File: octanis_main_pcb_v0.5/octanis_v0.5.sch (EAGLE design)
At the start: 80 parts, among them IC1 BME280, IC2 BNO055A, Q1 32.768kHz, Q2 32.768kHz, U1 MSP432, U2 TPS61232, U3 DRV8836DSSR, U4 DRV8836DSSR, U5 DRV8836DSSR, U6 DRV8836DSSR, U7 SST25VF064C

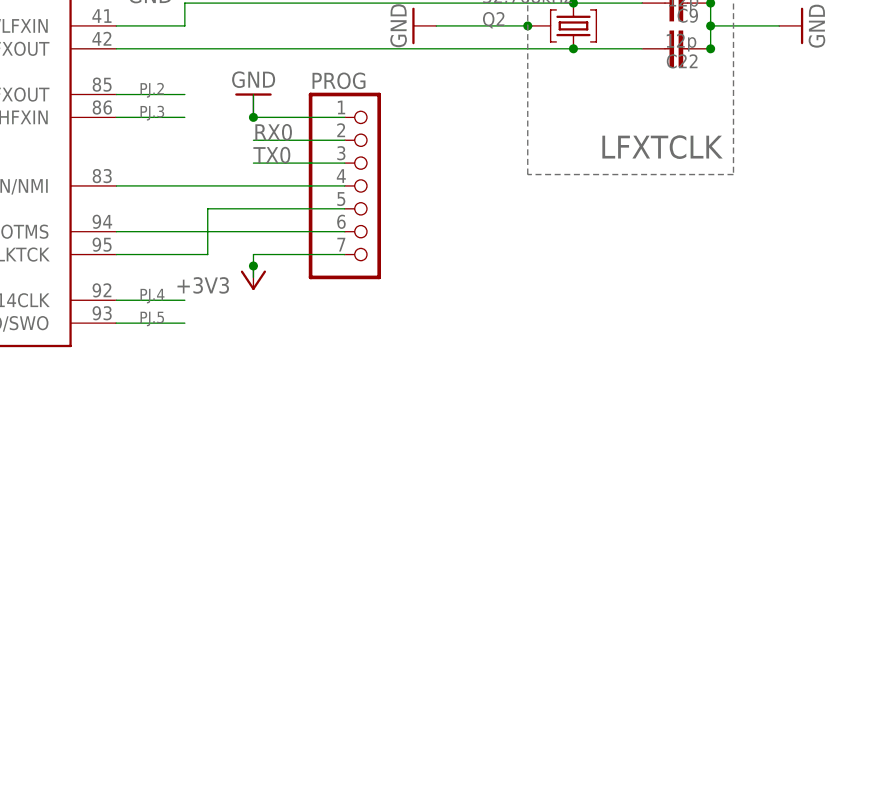
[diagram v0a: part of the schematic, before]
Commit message: added RST pull-up
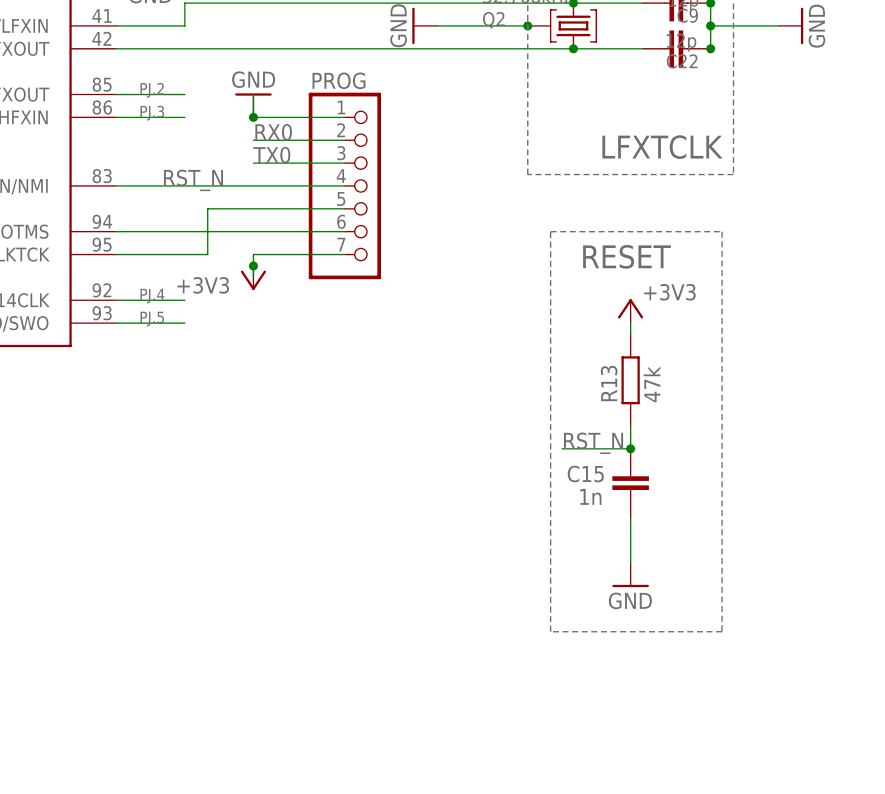
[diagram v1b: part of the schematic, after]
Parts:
- added C15: 1n, rcl:C-EUCM0402
- added R13: 47k, rcl:R-EU_RM0402
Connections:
- removed net N$75: PROG.4, U1.RSTN/NMI
- new net RST_N: C15.1, PROG.4, R13.1, U1.RSTN/NMI
- net +3V3: now also R13.2
- net GND: now also C15.2
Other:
- note added: "RESET"
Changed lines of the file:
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@@
 <part name="GND33" library="supply1" deviceset="GND" device=""/>
 <part name="GND34" library="supply1" deviceset="GND" device=""/>
+<part name="C15" library="rcl" deviceset="C-EU" device="CM0402" value="1n"/>
+<part name="GND40" library="supply1" deviceset="GND" device=""/>
+<part name="+3V25" library="supply1" deviceset="+3V3" device=""/>
+<part name="R13" library="rcl" deviceset="R-EU_" device="RM0402" value="47k"/>
 </parts>
 <sheets>
@@
 </text>
 <text x="228.6" y="228.6" size="1.27" layer="97">VeREF- (recommended to connect to GND)</text>
+<text x="424.942" y="188.976" size="2.54" layer="95">RESET</text>
+<wire x1="421.64" y1="148.59" x2="421.64" y2="193.04" width="0.1524" layer="95" style="shortdash"/>
+<wire x1="421.64" y1="193.04" x2="440.69" y2="193.04" width="0.1524" layer="95" style="shortdash"/>
+<wire x1="440.69" y1="193.04" x2="440.69" y2="148.59" width="0.1524" layer="95" style="shortdash"/>
+<wire x1="440.69" y1="148.59" x2="421.64" y2="148.59" width="0.1524" layer="95" style="shortdash"/>
 </plain>
 <instances>
@@
 <instance part="GND33" gate="1" x="205.74" y="215.9" rot="R90"/>
 <instance part="GND34" gate="1" x="266.7" y="228.6" rot="R270"/>
+<instance part="C15" gate="G$1" x="430.53" y="166.37" smashed="yes">
+<attribute name="NAME" x="423.418" y="165.227" size="1.778" layer="95"/>
+<attribute name="VALUE" x="424.688" y="162.687" size="1.778" layer="96"/>
+</instance>
+<instance part="GND40" gate="1" x="430.53" y="153.67"/>
+<instance part="+3V25" gate="G$1" x="430.53" y="185.42" smashed="yes">
+<attribute name="VALUE" x="431.8" y="185.42" size="1.778" layer="96"/>
+</instance>
+<instance part="R13" gate="G$1" x="430.53" y="176.53" smashed="yes" rot="R90">
+<attribute name="NAME" x="429.0314" y="173.99" size="1.778" layer="95" rot="R90"/>
+<attribute name="VALUE" x="433.832" y="173.99" size="1.778" layer="96" rot="R90"/>
+</instance>
 </instances>
 <busses>
@@
 <pinref part="GND8" gate="1" pin="GND"/>
 <wire x1="401.32" y1="299.72" x2="411.48" y2="299.72" width="0.1524" layer="91"/>
+</segment>
+<segment>
+<pinref part="GND40" gate="1" pin="GND"/>
+<pinref part="C15" gate="G$1" pin="2"/>
+<wire x1="430.53" y1="156.21" x2="430.53" y2="158.75" width="0.1524" layer="91"/>
+<wire x1="430.53" y1="158.75" x2="430.53" y2="161.29" width="0.1524" layer="91"/>
 </segment>
 </net>
@@
 <wire x1="398.78" y1="297.18" x2="411.48" y2="297.18" width="0.1524" layer="91"/>
 </segment>
+<segment>
+<pinref part="+3V25" gate="G$1" pin="+3V3"/>
+<wire x1="430.53" y1="182.88" x2="430.53" y2="181.61" width="0.1524" layer="91"/>
+<pinref part="R13" gate="G$1" pin="2"/>
+</segment>
 </net>
 <net name="M1IN2" class="0">
@@
 </segment>
 </net>
-<net name="N$75" class="0">
-<segment>
-<pinref part="U1" gate="MSP432" pin="RSTN/NMI"/>
-<wire x1="373.38" y1="198.12" x2="398.78" y2="198.12" width="0.1524" layer="91"/>
-<pinref part="PROG" gate="A" pin="4"/>
-</segment>
-</net>
 <net name="N$76" class="0">
 <segment>
@@
 </segment>
 </net>
+<net name="RST_N" class="0">
+<segment>
+<pinref part="C15" gate="G$1" pin="1"/>
+<wire x1="430.53" y1="168.91" x2="430.53" y2="171.45" width="0.1524" layer="91"/>
+<junction x="430.53" y="168.91"/>
+<pinref part="R13" gate="G$1" pin="1"/>
+<wire x1="430.53" y1="168.91" x2="422.91" y2="168.91" width="0.1524" layer="91"/>
+<label x="422.91" y="168.91" size="1.778" layer="95"/>
+</segment>
+<segment>
+<pinref part="U1" gate="MSP432" pin="RSTN/NMI"/>
+<wire x1="373.38" y1="198.12" x2="398.78" y2="198.12" width="0.1524" layer="91"/>
+<pinref part="PROG" gate="A" pin="4"/>
+<label x="378.46" y="198.12" size="1.778" layer="95"/>
+</segment>
+</net>

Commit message: added current sensors to motors on mainboard
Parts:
- removed ANALOG_IO: (no value), pinhead:PINHD-2X12
- added C21, C24, C31, C32: 10n, rcl:C-EUC0603
- added JP1: (no value), pinhead:PINHD-2X10
- added R_SENSE1, R_SENSE2, R_SENSE3, R_SENSE5: RSENSE1, Octanis1_EPS:CURRENT_RESISTOR
- added U$1, U$3, U$5, U$7: INA213, Octanis1_EPS:INA213
- RX2/TX2: device pinhead:PINHD-2X2 -> pinhead:PINHD-1X4
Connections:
- net AVCC1 renamed AVCC
- removed net A19: ANALOG_IO.20, U1.P8.6/A19
- removed net N$45 (its old number): SV3.1, U5.AOUT1
- removed net N$47: SV3.3, U5.BOUT1
- removed net N$53: SV4.1, U6.AOUT1
- removed net N$55: SV4.3, U6.BOUT1
- new net CURR_SENSE_EN: C21.2, C24.2, C31.2, C32.2, U$1.VCC, U$3.VCC, U$5.VCC, U$7.VCC, U1.P8.6/A19
- new net N$15: R_SENSE1.V2, U$1.IN-
- new net N$17: R_SENSE1.V1, U$1.IN+
- new net N$21: R_SENSE1.I2, SV3.1
- new net N$22: R_SENSE1.I1, U5.AOUT1
- new net N$23: R_SENSE5.V1, U$7.IN+
- new net N$24: R_SENSE5.V2, U$7.IN-
- new net N$25: R_SENSE5.I1, U5.BOUT1
- new net N$27: R_SENSE5.I2, SV3.3
- new net N$28: R_SENSE2.V2, U$3.IN-
- new net N$29: R_SENSE2.V1, U$3.IN+
- new net N$30: R_SENSE3.V2, U$5.IN-
- new net N$31: R_SENSE3.V1, U$5.IN+
- new net N$32: R_SENSE2.I2, SV4.1
- new net N$35: R_SENSE3.I1, U6.BOUT1
- new net N$36: R_SENSE2.I1, U6.AOUT1
- new net N$37: R_SENSE3.I2, SV4.3
- net +3V3: now also RX2/TX2.1; no longer RX2/TX2.3
- net +5V: now also MOT_J.2
- net A0: now also JP1.1; no longer ANALOG_IO.1
- net A1: now also JP1.2; no longer ANALOG_IO.2
- net A10: now also JP1.11; no longer ANALOG_IO.11
- net A11: now also JP1.12; no longer ANALOG_IO.12
- net A12: now also JP1.13; no longer ANALOG_IO.13
- net A13: now also JP1.14; no longer ANALOG_IO.14
- net A14: now also JP1.15; no longer ANALOG_IO.15
- net A15: now also JP1.16; no longer ANALOG_IO.16
- net A16: now also JP1.17; no longer ANALOG_IO.17
- net A17: now also JP1.18; no longer ANALOG_IO.18
- net A18: now also JP1.19; no longer ANALOG_IO.19
- net A2: now also JP1.3; no longer ANALOG_IO.3
- net A20: now also U$5.OUT; no longer ANALOG_IO.21
- net A21: now also U$3.OUT; no longer ANALOG_IO.22
- net A22: now also U$7.OUT; no longer ANALOG_IO.23
- net A23: now also U$1.OUT; no longer ANALOG_IO.24
- net A3: now also JP1.4; no longer ANALOG_IO.4
- net A4: now also JP1.5; no longer ANALOG_IO.5
- net A5: now also JP1.6; no longer ANALOG_IO.6
- net A6: now also JP1.7; no longer ANALOG_IO.7
- net A7: now also JP1.8; no longer ANALOG_IO.8
- net A8: now also JP1.9; no longer ANALOG_IO.9
- net A9: now also JP1.10; no longer ANALOG_IO.10
- net AGND: now also C21.1, C24.1, C31.1, C32.1, JP1.20, U$1.GND, U$1.REF, U$3.GND, U$3.REF, U$5.GND, U$5.REF, U$7.GND, U$7.REF
- net GND: now also RX2/TX2.4; no longer RX2/TX2.1
- net RX2: now also RX2/TX2.3; no longer RX2/TX2.2
- net TX2: now also RX2/TX2.2; no longer RX2/TX2.4
- net V_MOTOR: no longer MOT_J.2
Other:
- moved on the sheet: C26, C8, MOT_J, R11, RX2/TX2, SV3, SV4, U6

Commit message: silkscreen ready
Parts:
- RS1: value RSENSE1 -> RS1
- RS2: value RSENSE1 -> RS2
- RS3: value RSENSE1 -> RS3
- RS4: value RSENSE1 -> RS4
- renumbered JP1 to ANALOG, R_SENSE1 to RS1, R_SENSE2 to RS3, R_SENSE3 to RS4, R_SENSE5 to RS2, U$1 to U8, U$3 to U10, U$5 to U11, U$7 to U9

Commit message: added Vref and low pass filters for current sensors to mainboard
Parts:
- removed SV3, SV4: (no value), con-lstb:MA04-1
- added C33, C34, C35, C36: 470n, rcl:C-EUC0603
- added JP1, JP2: (no value), pinhead-2:PINHD-1X04_2.54-S
- added R14, R15, R17, R18: 6.8k, rcl:R-EU_R0603
- added U$3: MAX6001SOT-23, Octanis1:MAX6001SOT-23
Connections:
- net N$22 renamed M5OUT1
- new net A20UNF: R17.2, U11.OUT
- new net A21UNF: R18.2, U10.OUT
- new net A22UNF: R15.2, U9.OUT
- new net A23UNF: R14.2, U8.OUT
- new net VREF_M: U$3.OUT, U10.REF, U11.REF, U8.REF, U9.REF
- net +3V3: now also U$3.IN
- net A20: now also C35.2, R17.1; no longer U11.OUT
- net A21: now also C36.2, R18.1; no longer U10.OUT
- net A22: now also C34.2, R15.1; no longer U9.OUT
- net A23: now also C33.2, R14.1; no longer U8.OUT
- net AGND: now also C33.1, C34.1, C35.1, C36.1, U$3.GND; no longer U10.REF, U11.REF, U8.REF, U9.REF
- net M6IN1: now also U1.P8.0/UCB3STE/TA1.0/C0.1; no longer U1.P7.7/PM_TA1.1/C0.2
- net M6IN2: now also U1.P7.7/PM_TA1.1/C0.2; no longer U1.P8.0/UCB3STE/TA1.0/C0.1
- net N$21: now also JP1.1; no longer SV3.1
- net N$27: now also JP1.3; no longer SV3.3
- net N$32: now also JP2.1; no longer SV4.1
- net N$37: now also JP2.3; no longer SV4.3
- net N$38: now also JP1.2; no longer SV3.2
- net N$43: now also JP1.4; no longer SV3.4
- net N$45: now also JP2.4; no longer SV4.4
- net N$54: now also JP2.2; no longer SV4.2

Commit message: finised revised mainboard
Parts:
- removed SV1, SV2: (no value), con-lstb:MA04-1
- added M1/M2, M3/M4: (no value), pinhead-2:PINHD-1X04_2.54-S
- RX2/TX2: device pinhead:PINHD-1X4 -> pinhead-2:PINHD-1X04_2.54-S
- renumbered JP1 to M5/M6, JP2 to M7/M8, U$3 to U12
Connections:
- net N$13: now also M3/M4.1; no longer SV2.1
- net N$39: now also M3/M4.2; no longer SV2.2
- net N$40: now also M3/M4.3; no longer SV2.3
- net N$41: now also M3/M4.4; no longer SV2.4
- net N$49: now also M1/M2.1; no longer SV1.1
- net N$50: now also M1/M2.2; no longer SV1.2
- net N$51: now also M1/M2.3; no longer SV1.3
- net N$52: now also M1/M2.4; no longer SV1.4
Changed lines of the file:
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@@
 <part name="SUPPLY7" library="supply2" deviceset="GND" device=""/>
 <part name="U3" library="DRV8834" deviceset="DRV8836DSSR" device=""/>
-<part name="SV1" library="con-lstb" deviceset="MA04-1" device=""/>
 <part name="GND23" library="supply1" deviceset="GND" device=""/>
 <part name="SUPPLY5" library="supply2" deviceset="+5V" device=""/>
 <part name="SUPPLY6" library="supply2" deviceset="+5V" device=""/>
 <part name="U4" library="DRV8834" deviceset="DRV8836DSSR" device=""/>
-<part name="SV2" library="con-lstb" deviceset="MA04-1" device=""/>
 <part name="GND26" library="supply1" deviceset="GND" device=""/>
 <part name="U5" library="DRV8834" deviceset="DRV8836DSSR" device=""/>
@@
 <part name="AGND10" library="supply1" deviceset="AGND" device=""/>
 <part name="SUPPLY16" library="supply2" deviceset="+5V" device=""/>
-<part name="RX2/TX2" library="pinhead" deviceset="PINHD-1X4" device=""/>
-<part name="JP1" library="pinhead-2" deviceset="PINHD-1X04" device="_2.54-S"/>
-<part name="JP2" library="pinhead-2" deviceset="PINHD-1X04" device="_2.54-S"/>
-<part name="U$3" library="Octanis1" deviceset="MAX6001" device="SOT-23"/>
+<part name="M5/M6" library="pinhead-2" deviceset="PINHD-1X04" device="_2.54-S"/>
+<part name="M7/M8" library="pinhead-2" deviceset="PINHD-1X04" device="_2.54-S"/>
+<part name="U12" library="Octanis1" deviceset="MAX6001" device="SOT-23"/>
 <part name="+3V26" library="supply1" deviceset="+3V3" device=""/>
 <part name="AGND11" library="supply1" deviceset="AGND" device=""/>
@@
 <part name="C36" library="rcl" deviceset="C-EU" device="C0603" value="470n"/>
 <part name="AGND15" library="supply1" deviceset="AGND" device=""/>
+<part name="M3/M4" library="pinhead-2" deviceset="PINHD-1X04" device="_2.54-S"/>
+<part name="M1/M2" library="pinhead-2" deviceset="PINHD-1X04" device="_2.54-S"/>
+<part name="RX2/TX2" library="pinhead-2" deviceset="PINHD-1X04" device="_2.54-S"/>
 </parts>
 <sheets>
@@
 <instance part="SUPPLY7" gate="GND" x="406.4" y="396.24"/>
 <instance part="U3" gate="A" x="264.16" y="96.52"/>
-<instance part="SV1" gate="1" x="302.26" y="104.14" rot="R180"/>
 <instance part="GND23" gate="1" x="236.22" y="68.58"/>
 <instance part="SUPPLY5" gate="+5V" x="419.1" y="439.42"/>
 <instance part="SUPPLY6" gate="+5V" x="226.06" y="134.62"/>
 <instance part="U4" gate="A" x="360.68" y="96.52"/>
-<instance part="SV2" gate="1" x="398.78" y="104.14" rot="R180"/>
 <instance part="GND26" gate="1" x="332.74" y="68.58"/>
 <instance part="U5" gate="A" x="452.12" y="96.52"/>
@@
 <instance part="AGND10" gate="VR1" x="482.6" y="55.88" rot="MR90"/>
 <instance part="SUPPLY16" gate="+5V" x="408.94" y="111.76"/>
-<instance part="RX2/TX2" gate="A" x="233.68" y="287.02" rot="R180"/>
-<instance part="JP1" gate="A" x="520.7" y="104.14"/>
-<instance part="JP2" gate="A" x="698.5" y="104.14"/>
-<instance part="U$3" gate="G$1" x="558.8" y="165.1"/>
+<instance part="M5/M6" gate="A" x="520.7" y="104.14"/>
+<instance part="M7/M8" gate="A" x="698.5" y="104.14"/>
+<instance part="U12" gate="G$1" x="558.8" y="165.1"/>
 <instance part="+3V26" gate="G$1" x="546.1" y="170.18" smashed="yes">
 <attribute name="VALUE" x="543.56" y="170.18" size="1.778" layer="96"/>
@@
 </instance>
 <instance part="AGND15" gate="VR1" x="690.88" y="137.16" rot="R180"/>
+<instance part="M3/M4" gate="A" x="393.7" y="104.14"/>
+<instance part="M1/M2" gate="A" x="297.18" y="104.14"/>
+<instance part="RX2/TX2" gate="A" x="233.68" y="287.02" rot="R180"/>
 </instances>
 <busses>
@@
 </segment>
 <segment>
-<pinref part="RX2/TX2" gate="A" pin="4"/>
 <pinref part="GND31" gate="1" pin="GND"/>
 <wire x1="241.3" y1="289.56" x2="236.22" y2="289.56" width="0.1524" layer="91"/>
+<pinref part="RX2/TX2" gate="A" pin="4"/>
 </segment>
 </net>
@@
 <segment>
 <pinref part="U3" gate="A" pin="AOUT1"/>
-<pinref part="SV1" gate="1" pin="1"/>
 <wire x1="294.64" y1="109.22" x2="287.02" y2="109.22" width="0.1524" layer="91"/>
+<pinref part="M1/M2" gate="A" pin="1"/>
 </segment>
 </net>
@@
 <segment>
 <pinref part="U3" gate="A" pin="AOUT2"/>
-<pinref part="SV1" gate="1" pin="2"/>
 <wire x1="294.64" y1="106.68" x2="287.02" y2="106.68" width="0.1524" layer="91"/>
+<pinref part="M1/M2" gate="A" pin="2"/>
 </segment>
 </net>
@@
 <segment>
 <pinref part="U3" gate="A" pin="BOUT1"/>
-<pinref part="SV1" gate="1" pin="3"/>
 <wire x1="294.64" y1="104.14" x2="287.02" y2="104.14" width="0.1524" layer="91"/>
+<pinref part="M1/M2" gate="A" pin="3"/>
 </segment>
 </net>
@@
 <segment>
 <pinref part="U3" gate="A" pin="BOUT2"/>
-<pinref part="SV1" gate="1" pin="4"/>
 <wire x1="294.64" y1="101.6" x2="287.02" y2="101.6" width="0.1524" layer="91"/>
+<pinref part="M1/M2" gate="A" pin="4"/>
 </segment>
 </net>
@@
 </segment>
 <segment>
-<pinref part="RX2/TX2" gate="A" pin="1"/>
 <pinref part="+3V22" gate="G$1" pin="+3V3"/>
 <wire x1="243.84" y1="281.94" x2="236.22" y2="281.94" width="0.1524" layer="91"/>
-</segment>
-<segment>
-<pinref part="U$3" gate="G$1" pin="IN"/>
+<pinref part="RX2/TX2" gate="A" pin="1"/>
+</segment>
+<segment>
+<pinref part="U12" gate="G$1" pin="IN"/>
 <pinref part="+3V26" gate="G$1" pin="+3V3"/>
 <wire x1="546.1" y1="167.64" x2="551.18" y2="167.64" width="0.1524" layer="91"/>
@@
 <segment>
 <pinref part="U4" gate="A" pin="AOUT1"/>
-<pinref part="SV2" gate="1" pin="1"/>
 <wire x1="391.16" y1="109.22" x2="383.54" y2="109.22" width="0.1524" layer="91"/>
+<pinref part="M3/M4" gate="A" pin="1"/>
 </segment>
 </net>
@@
 <segment>
 <pinref part="U4" gate="A" pin="AOUT2"/>
-<pinref part="SV2" gate="1" pin="2"/>
 <wire x1="391.16" y1="106.68" x2="383.54" y2="106.68" width="0.1524" layer="91"/>
+<pinref part="M3/M4" gate="A" pin="2"/>
 </segment>
 </net>
@@
 <segment>
 <pinref part="U4" gate="A" pin="BOUT1"/>
-<pinref part="SV2" gate="1" pin="3"/>
 <wire x1="391.16" y1="104.14" x2="383.54" y2="104.14" width="0.1524" layer="91"/>
+<pinref part="M3/M4" gate="A" pin="3"/>
 </segment>
 </net>
@@
 <segment>
 <pinref part="U4" gate="A" pin="BOUT2"/>
-<pinref part="SV2" gate="1" pin="4"/>
 <wire x1="391.16" y1="101.6" x2="383.54" y2="101.6" width="0.1524" layer="91"/>
+<pinref part="M3/M4" gate="A" pin="4"/>
 </segment>
 </net>
@@
 <pinref part="U6" gate="A" pin="AOUT2"/>
 <wire x1="695.96" y1="106.68" x2="650.24" y2="106.68" width="0.1524" layer="91"/>
-<pinref part="JP2" gate="A" pin="2"/>
+<pinref part="M7/M8" gate="A" pin="2"/>
 </segment>
 </net>
@@
 </segment>
 <segment>
-<pinref part="U$3" gate="G$1" pin="GND"/>
+<pinref part="U12" gate="G$1" pin="GND"/>
 <wire x1="571.5" y1="165.1" x2="568.96" y2="165.1" width="0.1524" layer="91"/>
 <pinref part="AGND11" gate="VR1" pin="AGND"/>
@@
 <pinref part="RS1" gate="G$1" pin="I2"/>
 <wire x1="508" y1="109.22" x2="518.16" y2="109.22" width="0.1524" layer="91"/>
-<pinref part="JP1" gate="A" pin="1"/>
+<pinref part="M5/M6" gate="A" pin="1"/>
 </segment>
 </net>
@@
 <pinref part="U5" gate="A" pin="AOUT2"/>
 <wire x1="474.98" y1="106.68" x2="518.16" y2="106.68" width="0.1524" layer="91"/>
-<pinref part="JP1" gate="A" pin="2"/>
+<pinref part="M5/M6" gate="A" pin="2"/>
 </segment>
 </net>
@@
 <pinref part="RS2" gate="G$1" pin="I2"/>
 <wire x1="508" y1="104.14" x2="518.16" y2="104.14" width="0.1524" layer="91"/>
-<pinref part="JP1" gate="A" pin="3"/>
+<pinref part="M5/M6" gate="A" pin="3"/>
 </segment>
 </net>
@@
 <pinref part="U5" gate="A" pin="BOUT2"/>
 <wire x1="474.98" y1="101.6" x2="518.16" y2="101.6" width="0.1524" layer="91"/>
-<pinref part="JP1" gate="A" pin="4"/>
+<pinref part="M5/M6" gate="A" pin="4"/>
 </segment>
 </net>
@@
 <pinref part="RS3" gate="G$1" pin="I2"/>
 <wire x1="683.26" y1="109.22" x2="695.96" y2="109.22" width="0.1524" layer="91"/>
-<pinref part="JP2" gate="A" pin="1"/>
+<pinref part="M7/M8" gate="A" pin="1"/>
 </segment>
 </net>
@@
 <pinref part="RS4" gate="G$1" pin="I2"/>
 <wire x1="683.26" y1="104.14" x2="695.96" y2="104.14" width="0.1524" layer="91"/>
-<pinref part="JP2" gate="A" pin="3"/>
+<pinref part="M7/M8" gate="A" pin="3"/>
 </segment>
 </net>
@@
 <pinref part="U6" gate="A" pin="BOUT2"/>
 <wire x1="650.24" y1="101.6" x2="695.96" y2="101.6" width="0.1524" layer="91"/>
-<pinref part="JP2" gate="A" pin="4"/>
+<pinref part="M7/M8" gate="A" pin="4"/>
 </segment>
 </net>
@@
 </segment>
 <segment>
-<pinref part="U$3" gate="G$1" pin="OUT"/>
+<pinref part="U12" gate="G$1" pin="OUT"/>
 <wire x1="551.18" y1="162.56" x2="541.02" y2="162.56" width="0.1524" layer="91"/>
 <label x="541.02" y="162.56" size="1.778" layer="95"/>
